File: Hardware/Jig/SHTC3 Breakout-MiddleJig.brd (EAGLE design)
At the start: 25.4 x 25.4 mm, 33 parts, among them J3 PTH, U1 SHTC3

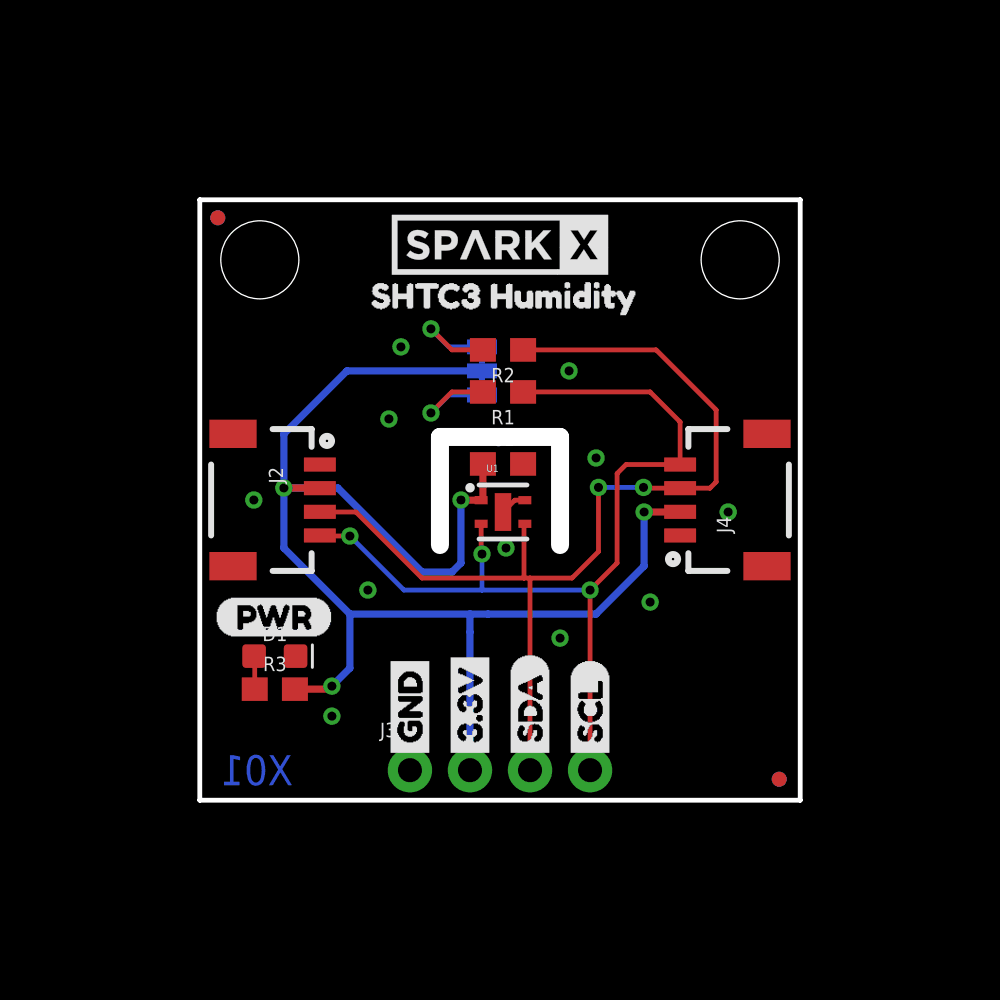
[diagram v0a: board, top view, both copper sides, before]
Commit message: Correcting HW Version
Looks like release version wasn't commited.  Updating.
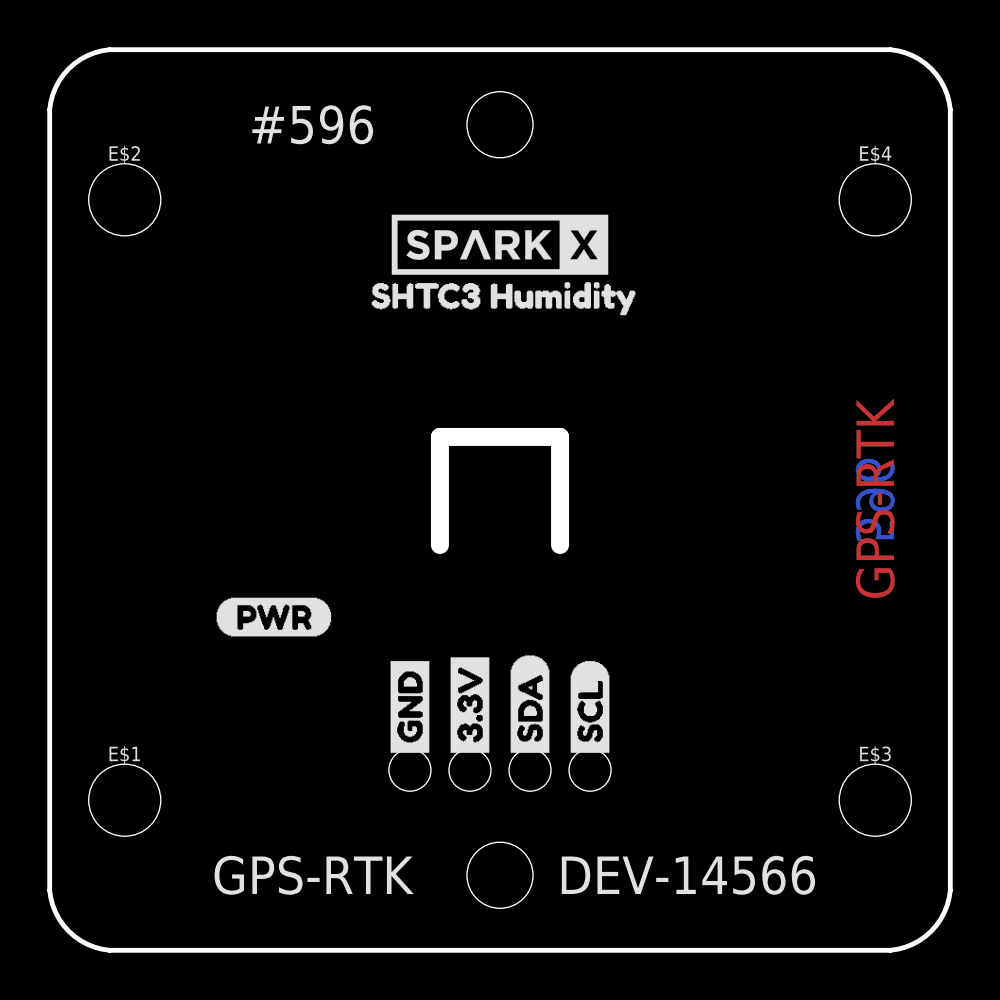
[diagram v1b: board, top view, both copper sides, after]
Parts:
- removed C1: 0.1uF, SparkFun-Capacitors:0603
- removed D1: RED, SparkFun-LED:LED-0603
- removed J2, J4: (no value), SparkFun-Connectors:1X04_1MM_RA
- removed J3: PTH, SparkX:1X04_NO_SILK
- removed JP1, JP2, JP5, JP6: FIDUCIALUFIDUCIAL, SparkFun:MICRO-FIDUCIAL
- removed JP3, JP4: STAND-OFF, SparkFun:STAND-OFF
- removed JP7: JUMPER-SMT_3_2-NC_TRACE_SILK, SparkFun-Jumpers:SMT-JUMPER_3_2-NC_TRACE_SILK
- removed R1, R2: 2.2k, SparkFun-Resistors:0603
- removed R3: 1k, SparkFun-Resistors:0603
- removed U1: SHTC3, SHTC3:SHTC3
- added E$1, E$2, E$3, E$4: (no value), SparkFun-Hardware:STAND-OFF-TIGHT
- added E$5, E$6: (no value), SparkFun-Hardware:NUBBIN_LOCKER
- moved FRAME1 57.2 mm to (44.5, -19.1)
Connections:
- removed net 3.3V: C1.1, J2.2, J3.2, J4.2, JP7.2, R3.2, U1.1
- removed net GND: C1.2, D1.C, J2.1, J3.1, J4.1, U1.4, U1.5
- removed net N$1: JP7.3, R1.2
- removed net N$2: JP7.1, R2.2
- removed net N$3: D1.A, R3.1
- removed net SCL: J2.4, J3.4, J4.4, R1.1, U1.2
- removed net SDA: J2.3, J3.3, J4.3, R2.1, U1.3
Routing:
- net 3.3V: track 62.7 -> 0.00 mm, vias 4 -> 0
- net SDA: track 43.9 -> 0.00 mm, vias 2 -> 0
- net SCL: track 40.0 -> 0.00 mm, vias 3 -> 0
- net N$2: track 5.04 -> 0.00 mm, vias 1 -> 0
- net N$1: track 5.04 -> 0.00 mm, vias 1 -> 0
- net N$3: track 1.41 -> 0.00 mm
- net GND: track 1.13 -> 0.00 mm, vias 11 -> 0
- removed copper zone on layer 1, net GND
- removed copper zone on layer 16, net GND
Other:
- board size 25.4 x 25.4 mm -> 38.1 x 38.1 mm
- board text added: "#596"
- board text added: "596"
- board text added: "DEV-14566"
- board text added: "GPS-RTK"
- board text removed: "X01"
